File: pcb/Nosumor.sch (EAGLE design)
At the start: 111 parts, among them IC1 STM32F722RET, IC2 REG1117, IC3 TPS77018, J3 SJ-43515TS-SMT-EDGE, K1 CHERRY-MX, K2 CHERRY-MX, K3 KSC623J, K4 KSC623J, K5 KSC623J, Q1 CX2016DB, Q2 ABMM-6.000MHZ, Q3 FDY100PZ, Q4 FDY100PZ, Q5 FDY100PZ, Q6 FDY100PZ, U2 USB3370, U3 TLV320AIC3110

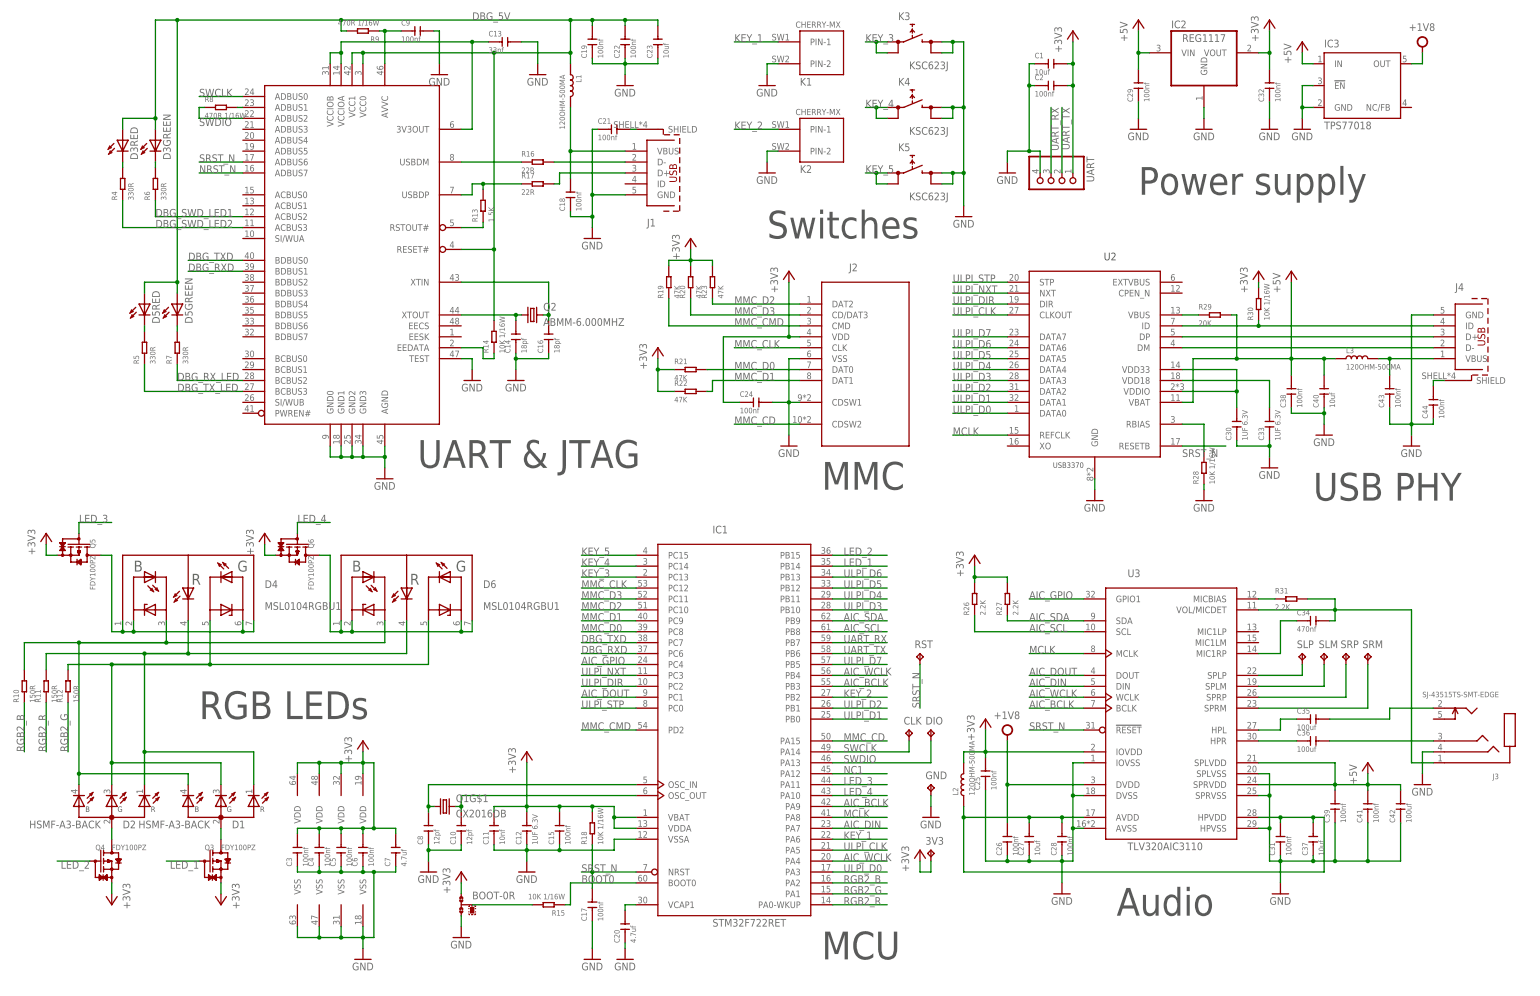
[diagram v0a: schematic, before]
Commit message: PCB: Connections done, update revision to 1.0
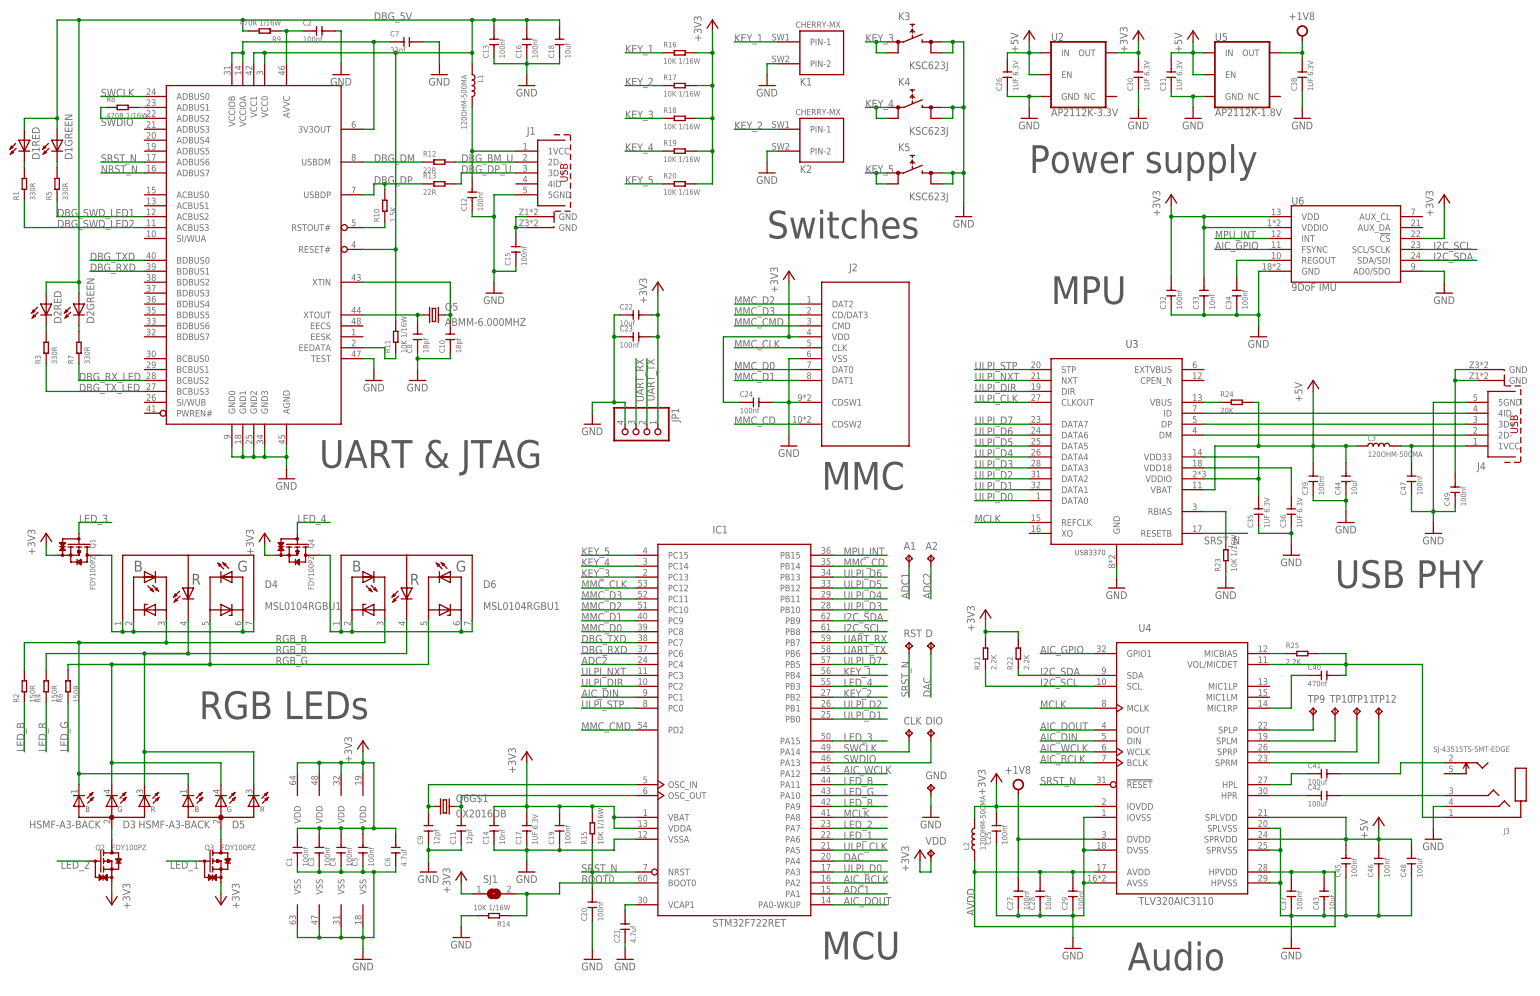
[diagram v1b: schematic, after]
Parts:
- removed BOOT: 0R-JUMPB, jump-0r-smd:0R-JUMPB
- removed IC2: REG1117, burr-brown:REG1117
- removed IC3: TPS77018, texas:TPS77018
- removed R26, R27, R31: 2.2K, Seeed-Resistor:SMD-RES-1K-5%-1/16W(0402)
- removed R28, R30: 10K 1/16W, Seeed-Resistor:SMD-RES-10K-1%-1/16W(0402)
- removed R29: 20K, Seeed-Resistor:SMD-RES-1K-5%-1/16W(0402)
- removed SLM, SLP, SRM, SRP: TPB1,27, testpad:TPB1,27
- removed UART: (no value), pinhead:PINHD-1X4
- added A1, A2, D, TP10, TP11, TP12, TP9: TPB1,27, testpad:TPB1,27
- added C45, C46, C47, C49: 100nf, Seeed-Capacitor:CERAMIC-100NF-25V-10%-X7R(0402)
- added C48: 100uf, Seeed-Capacitor:CERAMIC-100UF-6.3V-20%-X5R(1206)
- added JP1: (no value), pinhead:PINHD-1X4
- added R1, R3: 330R, Seeed-Resistor:SMD-RES-330R-1%-1/16W(0402)
- added R2: 150R, Seeed-Resistor:SMD-RES-330R-1%-1/16W(0402)
- added R24: 20K, Seeed-Resistor:SMD-RES-1K-5%-1/16W(0402)
- added R25: 2.2K, Seeed-Resistor:SMD-RES-1K-5%-1/16W(0402)
- added SJ1: (no value), jumper:SJ
- added U4: TLV320AIC3110, ti:TLV320AIC3110
- added U5: AP2112K-1.8V, SparkFun-IC-Power:V_REG_AP2112K-3.3V
- added U6: 9DoF IMU, SparkFun-Sensors:MPU-9250
- C1, C23, C27, C37: value 10uf -> 100nf; device Seeed-Capacitor:CERAMIC-10UF-10V-10%-X5R(0603) -> Seeed-Capacitor:CERAMIC-100NF-25V-10%-X7R(0402)
- C10, C8: value 12pf -> 18pf; device Seeed-Capacitor:CERAMIC-12PF-50V-5%-NPO(0402) -> Seeed-Capacitor:CERAMIC-18PF-50V-5%-NPO(0402)
- C11: value 10nf -> 12pf; device Seeed-Capacitor:CERAMIC-10NF-50V-10%-X7R(0402) -> Seeed-Capacitor:CERAMIC-12PF-50V-5%-NPO(0402)
- C12: value 1UF 6.3V -> 100nf; device Seeed-Capacitor:CERAMIC-1UF-6.3V-10%-X5R(0402) -> Seeed-Capacitor:CERAMIC-100NF-25V-10%-X7R(0402)
- C13: value 33nf -> 100nf; device Seeed-Capacitor:CERAMIC-22NF-50V-10%-X7R(0402) -> Seeed-Capacitor:CERAMIC-100NF-25V-10%-X7R(0402)
- C14: value 18pf -> 10nf; device Seeed-Capacitor:CERAMIC-18PF-50V-5%-NPO(0402) -> Seeed-Capacitor:CERAMIC-10NF-50V-10%-X7R(0402)
- C16: value 18pf -> 100nf; device Seeed-Capacitor:CERAMIC-18PF-50V-5%-NPO(0402) -> Seeed-Capacitor:CERAMIC-100NF-25V-10%-X7R(0402)
- C17, C26, C31, C38: value 100nf -> 1UF 6.3V; device Seeed-Capacitor:CERAMIC-100NF-25V-10%-X7R(0402) -> Seeed-Capacitor:CERAMIC-1UF-6.3V-10%-X5R(0402)
- C18, C22, C28, C43, C44: value 100nf -> 10uf; device Seeed-Capacitor:CERAMIC-100NF-25V-10%-X7R(0402) -> Seeed-Capacitor:CERAMIC-10UF-10V-10%-X5R(0603)
- C20: value 4.7uf -> 100nf; device Seeed-Capacitor:CERAMIC-4.7UF-10V-10%-X5R(0603) -> Seeed-Capacitor:CERAMIC-100NF-25V-10%-X7R(0402)
- C21, C6: value 100nf -> 4.7uf; device Seeed-Capacitor:CERAMIC-100NF-25V-10%-X7R(0402) -> Seeed-Capacitor:CERAMIC-4.7UF-10V-10%-X5R(0603)
- C33: value 1UF 6.3V -> 10nf; device Seeed-Capacitor:CERAMIC-1UF-6.3V-10%-X5R(0402) -> Seeed-Capacitor:CERAMIC-10NF-50V-10%-X7R(0402)
- C34: value 470nf -> 100nf; device Seeed-Capacitor:CERAMIC-47NF-25V-10%-X7R(0402) -> Seeed-Capacitor:CERAMIC-100NF-25V-10%-X7R(0402)
- C35, C36: value 100uf -> 1UF 6.3V; device Seeed-Capacitor:CERAMIC-100UF-6.3V-20%-X5R(1206) -> Seeed-Capacitor:CERAMIC-1UF-6.3V-10%-X5R(0402)
- C40: value 10uf -> 470nf; device Seeed-Capacitor:CERAMIC-10UF-10V-10%-X5R(0603) -> Seeed-Capacitor:CERAMIC-47NF-25V-10%-X7R(0402)
- C41: value 100nf -> 100uf; device Seeed-Capacitor:CERAMIC-100NF-25V-10%-X7R(0402) -> Seeed-Capacitor:CERAMIC-100UF-6.3V-20%-X5R(1206)
- C7: value 4.7uf -> 33nf; device Seeed-Capacitor:CERAMIC-4.7UF-10V-10%-X5R(0603) -> Seeed-Capacitor:CERAMIC-22NF-50V-10%-X7R(0402)
- C9: value 100nf -> 12pf; device Seeed-Capacitor:CERAMIC-100NF-25V-10%-X7R(0402) -> Seeed-Capacitor:CERAMIC-12PF-50V-5%-NPO(0402)
- D1, D2: value HSMF-A3-BACK -> APBD3224SURKCGKC-F01; device led:HSMF-A3-BACK -> led:APBD3224SURKCGKC-F01
- D3, D5: value APBD3224SURKCGKC-F01 -> HSMF-A3-BACK; device led:APBD3224SURKCGKC-F01 -> led:HSMF-A3-BACK
- J1, J4: device Wurth_Elektronik_Electromechanic_Input-Output_Connectors_rev17b:629105136821 -> Wurth_Elektronik_Electromechanic_Input-Output_Connectors_rev16b:629105150521
- Q1: value CX2016DB -> FDY100PZ; device crystal:CX2016DB -> transistor:FDY100PZ
- Q2: value ABMM-6.000MHZ -> FDY100PZ; device crystal:ABMM-6.000MHZ -> transistor:FDY100PZ
- Q5: value FDY100PZ -> ABMM-6.000MHZ; device transistor:FDY100PZ -> crystal:ABMM-6.000MHZ
- Q6: value FDY100PZ -> CX2016DB; device transistor:FDY100PZ -> crystal:CX2016DB
- R10: value 150R -> 1.5K; device Seeed-Resistor:SMD-RES-330R-1%-1/16W(0402) -> Seeed-Resistor:SMD-RES-1.5K-5%-1/16W(0402)
- R11: value 150R -> 10K 1/16W; device Seeed-Resistor:SMD-RES-330R-1%-1/16W(0402) -> Seeed-Resistor:SMD-RES-10K-1%-1/16W(0402)
- R12: value 150R -> 22R; device Seeed-Resistor:SMD-RES-330R-1%-1/16W(0402) -> Seeed-Resistor:SMD-RES-22R-1%-1/16W(0402)
- R13: value 1.5K -> 22R; device Seeed-Resistor:SMD-RES-1.5K-5%-1/16W(0402) -> Seeed-Resistor:SMD-RES-22R-1%-1/16W(0402)
- R16, R17: value 22R -> 10K 1/16W; device Seeed-Resistor:SMD-RES-22R-1%-1/16W(0402) -> Seeed-Resistor:SMD-RES-10K-1%-1/16W(0402)
- R19, R20, R23: value 47K -> 10K 1/16W; device Seeed-Resistor:SMD-RES-47K-5%-1/16W(0402) -> Seeed-Resistor:SMD-RES-10K-1%-1/16W(0402)
- R21, R22: value 47K -> 2.2K; device Seeed-Resistor:SMD-RES-47K-5%-1/16W(0402) -> Seeed-Resistor:SMD-RES-1K-5%-1/16W(0402)
- R4, R6: value 330R -> 150R
- U2: value USB3370 -> AP2112K-3.3V; device microchip:USB3370 -> SparkFun-IC-Power:V_REG_AP2112K-3.3V
- U3: value TLV320AIC3110 -> USB3370; device ti:TLV320AIC3110 -> microchip:USB3370
- renumbered 3V3 to VDD
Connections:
- removed net AIC_SCL: IC1G$1.PB8, R26.1, U3.SCL
- removed net AIC_SDA: IC1G$1.PB9, R27.1, U3.SDA
- removed net N$15: R16.1, U1.USBDM
- removed net N$16: J1.D+, R17.2
- removed net N$22: C21.2, J1.SHIELD
- removed net N$40: D1.KG, D2.KG, D4.KB, D6.KB, R12.2
- removed net N$41: D1.KR, D2.KR, D4.KR, D6.KR, R11.2
- removed net N$42: D1.KB, D2.KB, D4.KG, D6.KG, R10.2
- removed net N$51: C27.2, C28.2, C31.2, C37.2, L2.1, U3.AVDD, U3.HPVDD
- removed net N$8: J1.D-, R16.2
- removed net N$9: R13.2, R17.1, U1.USBDP
- removed net NC1: IC1G$1.PA12
- removed net RGB2_B: IC1G$1.PA2, R10.1
- removed net RGB2_G: IC1G$1.PA1, R12.1
- removed net RGB2_R: IC1G$1.PA0-WKUP, R11.1
- new net ADC1: A1.TP, IC1G$1.PA1
- new net ADC2: A2.TP, IC1G$1.PC4
- new net AVDD: C28.2, C29.2, C37.2, C43.2, L2.1, U4.AVDD, U4.HPVDD
- new net DAC: D.TP, IC1G$1.PA4
- new net DBG_BM_U: J1.2D-, R12.2
- new net DBG_DM: R12.1, U1.USBDM
- new net DBG_DP: R10.2, R13.1, U1.USBDP
- new net DBG_DP_U: J1.3D+, R13.2
- new net I2C_SCL: IC1G$1.PB8, R21.1, U4.SCL, U6.SCL/SCLK
- new net I2C_SDA: IC1G$1.PB9, R22.1, U4.SDA, U6.SDA/SDI
- new net LED_B: IC1G$1.PA11, R2.1
- new net LED_G: IC1G$1.PA10, R6.1
- new net LED_R: IC1G$1.PA9, R4.1
- new net MPU_INT: IC1G$1.PB15, U6.INT
- new net N$47: C34.2, U6.REGOUT
- new net RGB_B: D3.KB, D4.KG, D5.KB, D6.KG, R2.2
- new net RGB_G: D3.KG, D4.KB, D5.KG, D6.KB, R6.2
- new net RGB_R: D3.KR, D4.KR, D5.KR, D6.KR, R4.2
- net +1V8: now also C27.2, C38.2, U4.DVDD, U5.OUT; no longer C26.2, IC3.OUT, U3.DVDD
- net +3V3: now also C14.2, C17.2, C19.2, C22.2, C23.2, C30.2, C33.2, JP1.1, Q1.S, Q2.S, R15.2, R16.2, R17.2, R21.2, R22.2, SJ1.1, U2.OUT, U4.IOVDD, U6.!CS, U6.VDD, U6.VDDIO; no longer BOOT-0R.1, C11.2, C12.2, C15.2, C2.2, C7.2, IC2.VOUT, Q5.S, Q6.S, R21.1, R22.1, R23.2, R26.2, R27.2, R30.2, U3.IOVDD, UART.1
- net +5V: now also C26.2, C31.2, C44.2, C45.2, C46.2, C48.2, R24.2, U2.EN, U2.IN, U3.VBAT, U4.SPLVDD, U4.SPRVDD, U5.EN, U5.IN; no longer C29.2, C38.2, C40.2, C41.2, C42.2, IC2.VIN, IC3.IN, R29.2, U2.VBAT, U3.SPLVDD, U3.SPRVDD
- net AIC_BCLK: now also IC1G$1.PA2, U4.BCLK; no longer IC1G$1.PA9, IC1G$1.PB3, U3.BCLK
- net AIC_DIN: now also IC1G$1.PC1, U4.DIN; no longer IC1G$1.PA7, U3.DIN
- net AIC_DOUT: now also IC1G$1.PA0-WKUP, U4.DOUT; no longer IC1G$1.PC1, U3.DOUT
- net AIC_GPIO: now also U4.GPIO1, U6.FSYNC; no longer IC1G$1.PC4, U3.GPIO1
- net AIC_WCLK: now also IC1G$1.PA12, U4.WCLK; no longer IC1G$1.PA4, IC1G$1.PB4, U3.WCLK
- net BOOT0: now also R14.1, SJ1.2; no longer R15.1
- net DBG_5V: now also C13.2, C16.2, C18.2, D1GREEN.A, D1RED.A, D2GREEN.A, D2RED.A, R11.2; no longer C19.2, C22.2, C23.2, D3GREEN.A, D3RED.A, D5GREEN.A, D5RED.A, R14.2
- net DBG_SWD_LED1: now also R5.1; no longer R6.1
- net DBG_SWD_LED2: now also R1.1; no longer R4.1
- net DBG_TX_LED: now also R3.1; no longer R5.1
- net GND: now also C13.1, C2.2, C34.1, C35.1, C36.1, C45.1, C46.1, C47.1, C48.1, C49.1, C7.2, C9.1, J1.5GND, J4.5GND, JP1.4, R14.2, R23.1, U3.GND, U4.AVSS, U4.DVSS, U4.HPVSS, U4.IOVSS, U4.SPLVSS, U4.SPRVSS, U5.GND, U6.AD0/SDO, U6.GND; no longer BOOT-0R.3, C13.2, C2.1, C40.1, C41.1, C42.1, C7.1, C9.2, IC2.GND, IC3.!EN, IC3.GND, J1.GND, J4.GND, R28.1, U3.AVSS, U3.DVSS, U3.HPVSS, U3.IOVSS, U3.SPLVSS, U3.SPRVSS, UART.4
- net KEY_1: now also IC1G$1.PB4, R16.1; no longer IC1G$1.PA6
- net KEY_2: now also R17.1
- net KEY_3: now also R18.1
- net KEY_4: now also R19.1
- net KEY_5: now also R20.1
- net LED_1: now also IC1G$1.PA6; no longer IC1G$1.PB14
- net LED_2: now also IC1G$1.PA7, Q2.G; no longer IC1G$1.PB15, Q4.G
- net LED_3: now also IC1G$1.PA15, Q1.G; no longer IC1G$1.PA11, Q5.G
- net LED_4: now also IC1G$1.PB3, Q4.G; no longer IC1G$1.PA10, Q6.G
- net MCLK: now also U3.REFCLK, U4.MCLK; no longer U2.REFCLK, U3.MCLK
- net MMC_CD: now also IC1G$1.PB14; no longer IC1G$1.PA15
- net MMC_CMD: no longer R19.1
- net MMC_D0: no longer R21.2
- net MMC_D1: no longer R22.2
- net MMC_D2: no longer R23.1
- net MMC_D3: no longer R20.1
- net N$1: now also C41.2; no longer C35.2
- net N$10: now also C7.1; no longer C13.1
- net N$11: now also C2.1; no longer C9.1
- net N$12: now also D1GREEN.C, R5.2; no longer D3GREEN.C, R6.2
- net N$13: now also C12.2, J1.1VCC; no longer C18.2, J1.VBUS
- net N$14: now also R10.1; no longer R13.1
- net N$17: now also R11.1; no longer R14.1
- net N$18: now also C8.2, Q5.1; no longer C14.2, Q2.1
- net N$19: now also C10.2, Q5.2; no longer C16.2, Q2.2
- net N$2: now also C42.2; no longer C36.2
- net N$20: now also D2GREEN.C; no longer D5GREEN.C
- net N$21: now also D2RED.C, R3.2; no longer D5RED.C, R5.2
- net N$23: now also D1RED.C, R1.2; no longer D3RED.C, R4.2
- net N$24: now also C9.2, Q6G$1.1; no longer C8.2, Q1G$1.1
- net N$26: now also C11.2, Q6G$1.2; no longer C10.2, Q1G$1.2
- net N$27: now also C15.2, J1.GND@1, J1.GND@2; no longer BOOT-0R.2, R15.2
- net N$28: now also Q4.D; no longer Q6.D
- net N$29: now also C21.2; no longer C20.2
- net N$3: now also C40.2, R25.2, U4.VOL/MICDET; no longer C34.2, R31.2, U3.VOL/MICDET
- net N$30: now also TP10.TP, U4.SPLM; no longer SLM.TP, U3.SPLM
- net N$31: now also C47.2, J4.1VCC; no longer C43.2, J4.VBUS
- net N$32: now also R24.1, U3.VBUS; no longer R29.1, U2.VBUS
- net N$33: now also C35.2, U3.VDD33, U3.VDDIO; no longer C30.2, U2.VDD33, U2.VDDIO
- net N$34: now also D5.A; no longer D1.A
- net N$35: now also C49.2, J4.GND@1, J4.GND@2; no longer C44.2, J4.SHIELD
- net N$36: now also C36.2, U3.VDD18; no longer C33.2, U2.VDD18
- net N$37: now also R23.2, U3.RBIAS; no longer R28.2, U2.RBIAS
- net N$38: now also Q1.D; no longer Q5.D
- net N$39: now also D3.A, Q2.D; no longer D2.A, Q4.D
- net N$4: now also J4.2D-, U3.DM; no longer J4.D+, U2.DP
- net N$44: now also TP11.TP, U4.SPRP; no longer SRP.TP, U3.SPRP
- net N$45: now also TP12.TP, U4.SPRM; no longer SRM.TP, U3.SPRM
- net N$46: now also C40.1, U4.MIC1RP; no longer C34.1, U3.MIC1RP
- net N$48: now also C42.1, U4.HPR; no longer C36.1, U3.HPR
- net N$49: now also R25.1, U4.MICBIAS; no longer R31.1, U3.MICBIAS
- net N$5: now also J4.3D+, U3.DP; no longer J4.D-, U2.DM
- net N$50: now also C41.1, U4.HPL; no longer C35.1, U3.HPL
- net N$6: now also J4.4ID, U3.ID; no longer J4.ID, R30.1, U2.ID
- net N$7: now also TP9.TP, U4.SPLP; no longer SLP.TP, U3.SPLP
- net SRST_N: now also C20.2, R15.1, U3.RESETB, U4.!RESET; no longer C17.2, R18.1, U2.RESETB, U3.!RESET
- net UART_RX: now also JP1.3; no longer UART.3
- net UART_TX: now also JP1.2; no longer UART.2
- net ULPI_CLK: now also U3.CLKOUT; no longer U2.CLKOUT
- net ULPI_D0: now also U3.DATA0; no longer U2.DATA0
- net ULPI_D1: now also U3.DATA1; no longer U2.DATA1
- net ULPI_D2: now also U3.DATA2; no longer U2.DATA2
- net ULPI_D3: now also U3.DATA3; no longer U2.DATA3
- net ULPI_D4: now also U3.DATA4; no longer U2.DATA4
- net ULPI_D5: now also U3.DATA5; no longer U2.DATA5
- net ULPI_D6: now also U3.DATA6; no longer U2.DATA6
- net ULPI_D7: now also U3.DATA7; no longer U2.DATA7
- net ULPI_DIR: now also U3.DIR; no longer U2.DIR
- net ULPI_NXT: now also U3.NXT; no longer U2.NXT
- net ULPI_STP: now also U3.STP; no longer U2.STP
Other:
- note added: "MPU"
- moved on the sheet: C1, C10, C11, C12, C13, C14, C15, C16, C17, C18, C19, C2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

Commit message: PCB: Revision 1.0, silkscreen checked
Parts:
- added GND$2, SCL, SDA: TPB1,27, testpad:TPB1,27
- renumbered SJ1 to BOOT, TP10 to SLM, TP11 to SRP, TP12 to SRM, TP9 to SLP
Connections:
- net GND: now also GND$2.TP
- net I2C_SCL: now also SCL.TP
- net I2C_SDA: now also SDA.TP
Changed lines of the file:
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@@
 <part name="P+2" library="supply1" library_urn="urn:adsk.eagle:library:371" deviceset="+5V" device=""/>
 <part name="V2" library="supply" deviceset="+1V8" device=""/>
-<part name="TP9" library="testpad" library_urn="urn:adsk.eagle:library:385" deviceset="TP" device="B1,27" package3d_urn="urn:adsk.eagle:package:27944/1"/>
-<part name="TP10" library="testpad" library_urn="urn:adsk.eagle:library:385" deviceset="TP" device="B1,27" package3d_urn="urn:adsk.eagle:package:27944/1"/>
-<part name="TP11" library="testpad" library_urn="urn:adsk.eagle:library:385" deviceset="TP" device="B1,27" package3d_urn="urn:adsk.eagle:package:27944/1"/>
-<part name="TP12" library="testpad" library_urn="urn:adsk.eagle:library:385" deviceset="TP" device="B1,27" package3d_urn="urn:adsk.eagle:package:27944/1"/>
+<part name="SLP" library="testpad" library_urn="urn:adsk.eagle:library:385" deviceset="TP" device="B1,27" package3d_urn="urn:adsk.eagle:package:27944/1"/>
+<part name="SLM" library="testpad" library_urn="urn:adsk.eagle:library:385" deviceset="TP" device="B1,27" package3d_urn="urn:adsk.eagle:package:27944/1"/>
+<part name="SRP" library="testpad" library_urn="urn:adsk.eagle:library:385" deviceset="TP" device="B1,27" package3d_urn="urn:adsk.eagle:package:27944/1"/>
+<part name="SRM" library="testpad" library_urn="urn:adsk.eagle:library:385" deviceset="TP" device="B1,27" package3d_urn="urn:adsk.eagle:package:27944/1"/>
 <part name="C40" library="Seeed-Capacitor" library_urn="urn:adsk.eagle:library:464" deviceset="CERAMIC-47NF-25V-10%-X7R(0402)" device="" value="470nf"/>
 <part name="R25" library="Seeed-Resistor" library_urn="urn:adsk.eagle:library:474" deviceset="SMD-RES-1K-5%-1/16W(0402)" device="" value="2.2K"/>
@@
 <part name="R16" library="Seeed-Resistor" library_urn="urn:adsk.eagle:library:474" deviceset="SMD-RES-10K-1%-1/16W(0402)" device="" value="10K 1/16W"/>
 <part name="+3V39" library="supply1" library_urn="urn:adsk.eagle:library:371" deviceset="+3V3" device=""/>
-<part name="SJ1" library="jumper" library_urn="urn:adsk.eagle:library:252" deviceset="SJ" device="" package3d_urn="urn:adsk.eagle:package:15471/1"/>
+<part name="BOOT" library="jumper" library_urn="urn:adsk.eagle:library:252" deviceset="SJ" device="" package3d_urn="urn:adsk.eagle:package:15471/1"/>
 <part name="J4" library="Wurth_Elektronik_Electromechanic_Input-Output_Connectors_rev16b" deviceset="629105150521" device=""/>
 <part name="J1" library="Wurth_Elektronik_Electromechanic_Input-Output_Connectors_rev16b" deviceset="629105150521" device=""/>
@@
 <part name="GND29" library="supply1" library_urn="urn:adsk.eagle:library:371" deviceset="GND" device=""/>
 <part name="C31" library="Seeed-Capacitor" library_urn="urn:adsk.eagle:library:464" deviceset="CERAMIC-1UF-6.3V-10%-X5R(0402)" device="" value="1UF 6.3V"/>
+<part name="SDA" library="testpad" library_urn="urn:adsk.eagle:library:385" deviceset="TP" device="B1,27" package3d_urn="urn:adsk.eagle:package:27944/1"/>
+<part name="SCL" library="testpad" library_urn="urn:adsk.eagle:library:385" deviceset="TP" device="B1,27" package3d_urn="urn:adsk.eagle:package:27944/1"/>
+<part name="GND$2" library="testpad" library_urn="urn:adsk.eagle:library:385" deviceset="TP" device="B1,27" package3d_urn="urn:adsk.eagle:package:27944/1"/>
 </parts>
 <sheets>
@@
 <instance part="P+2" gate="1" x="86.36" y="111.76"/>
 <instance part="V2" gate="G$1" x="111.76" y="111.76"/>
-<instance part="TP9" gate="G$1" x="114.3" y="-45.72"/>
-<instance part="TP10" gate="G$1" x="119.38" y="-45.72"/>
-<instance part="TP11" gate="G$1" x="124.46" y="-45.72"/>
-<instance part="TP12" gate="G$1" x="129.54" y="-45.72"/>
+<instance part="SLP" gate="G$1" x="114.3" y="-45.72"/>
+<instance part="SLM" gate="G$1" x="119.38" y="-45.72"/>
+<instance part="SRP" gate="G$1" x="124.46" y="-45.72"/>
+<instance part="SRM" gate="G$1" x="129.54" y="-45.72"/>
 <instance part="C40" gate="G$1" x="116.84" y="-38.1"/>
 <instance part="R25" gate="G$1" x="111.76" y="-33.02"/>
@@
 <instance part="R16" gate="G$1" x="-33.02" y="106.68"/>
 <instance part="+3V39" gate="G$1" x="-25.4" y="114.3"/>
-<instance part="SJ1" gate="1" x="-76.2" y="-88.9"/>
+<instance part="BOOT" gate="1" x="-76.2" y="-88.9"/>
 <instance part="J4" gate="G$1" x="157.48" y="20.32" rot="MR180"/>
 <instance part="J1" gate="G$1" x="-63.5" y="78.74"/>
@@
 <instance part="GND29" gate="1" x="111.76" y="91.44"/>
 <instance part="C31" gate="G$1" x="81.28" y="101.6" rot="R90"/>
+<instance part="SDA" gate="G$1" x="-50.8" y="10.16"/>
+<instance part="SCL" gate="G$1" x="-43.18" y="10.16"/>
+<instance part="GND$2" gate="G$1" x="-35.56" y="10.16"/>
 </instances>
 <busses>
@@
 <pinref part="C38" gate="G$1" pin="1"/>
 </segment>
+<segment>
+<pinref part="GND$2" gate="G$1" pin="TP"/>
+<wire x1="-35.56" y1="7.62" x2="-35.56" y2="-2.54" width="0.1524" layer="91"/>
+<label x="-35.56" y="-2.54" size="1.778" layer="95" rot="R90"/>
+</segment>
 </net>
 <net name="+3V3" class="0">
@@
 <pinref part="+3V36" gate="G$1" pin="+3V3"/>
 <wire x1="-83.82" y1="-88.9" x2="-83.82" y2="-86.36" width="0.1524" layer="91"/>
-<pinref part="SJ1" gate="1" pin="1"/>
+<pinref part="BOOT" gate="1" pin="1"/>
 <wire x1="-81.28" y1="-88.9" x2="-83.82" y2="-88.9" width="0.1524" layer="91"/>
 </segment>
@@
 <label x="-55.88" y="-86.36" size="1.778" layer="95"/>
 <wire x1="-60.96" y1="-86.36" x2="-60.96" y2="-88.9" width="0.1524" layer="91"/>
-<pinref part="SJ1" gate="1" pin="2"/>
+<pinref part="BOOT" gate="1" pin="2"/>
 <wire x1="-71.12" y1="-88.9" x2="-68.58" y2="-88.9" width="0.1524" layer="91"/>
 <wire x1="-68.58" y1="-88.9" x2="-68.58" y2="-93.98" width="0.1524" layer="91"/>
@@
 <net name="N$7" class="0">
 <segment>
-<pinref part="TP9" gate="G$1" pin="TP"/>
+<pinref part="SLP" gate="G$1" pin="TP"/>
 <wire x1="114.3" y1="-48.26" x2="114.3" y2="-50.8" width="0.1524" layer="91"/>
 <pinref part="U4" gate="G$1" pin="SPLP"/>
@@
 <segment>
 <pinref part="U4" gate="G$1" pin="SPLM"/>
-<pinref part="TP10" gate="G$1" pin="TP"/>
+<pinref part="SLM" gate="G$1" pin="TP"/>
 <wire x1="104.14" y1="-53.34" x2="119.38" y2="-53.34" width="0.1524" layer="91"/>
 <wire x1="119.38" y1="-53.34" x2="119.38" y2="-48.26" width="0.1524" layer="91"/>
@@
 <segment>
 <pinref part="U4" gate="G$1" pin="SPRP"/>
-<pinref part="TP11" gate="G$1" pin="TP"/>
+<pinref part="SRP" gate="G$1" pin="TP"/>
 <wire x1="104.14" y1="-55.88" x2="124.46" y2="-55.88" width="0.1524" layer="91"/>
 <wire x1="124.46" y1="-55.88" x2="124.46" y2="-48.26" width="0.1524" layer="91"/>
@@
 <segment>
 <pinref part="U4" gate="G$1" pin="SPRM"/>
-<pinref part="TP12" gate="G$1" pin="TP"/>
+<pinref part="SRM" gate="G$1" pin="TP"/>
 <wire x1="104.14" y1="-58.42" x2="129.54" y2="-58.42" width="0.1524" layer="91"/>
 <wire x1="129.54" y1="-58.42" x2="129.54" y2="-48.26" width="0.1524" layer="91"/>
@@
 <label x="142.24" y="58.42" size="1.778" layer="95"/>
 </segment>
+<segment>
+<pinref part="SDA" gate="G$1" pin="TP"/>
+<wire x1="-50.8" y1="7.62" x2="-50.8" y2="-2.54" width="0.1524" layer="91"/>
+<label x="-50.8" y="-2.54" size="1.778" layer="95" rot="R90"/>
+</segment>
 </net>
 <net name="I2C_SCL" class="0">
@@
 <label x="142.24" y="60.96" size="1.778" layer="95"/>
 </segment>
+<segment>
+<pinref part="SCL" gate="G$1" pin="TP"/>
+<wire x1="-43.18" y1="7.62" x2="-43.18" y2="-2.54" width="0.1524" layer="91"/>
+<label x="-43.18" y="-2.54" size="1.778" layer="95" rot="R90"/>
+</segment>
 </net>
 <net name="AIC_DOUT" class="0">
@@
 <wire x1="104.14" y1="60.96" x2="91.44" y2="60.96" width="0.1524" layer="91"/>
 <label x="91.44" y="60.96" size="1.778" layer="95"/>
+<wire x1="104.14" y1="60.96" x2="91.44" y2="60.96" width="0.1524" layer="91"/>
 </segment>
 </net>
@@
 <wire x1="104.14" y1="63.5" x2="91.44" y2="63.5" width="0.1524" layer="91"/>
 <label x="91.44" y="63.5" size="1.778" layer="95"/>
-</segment>
-<segment>
+<wire x1="104.14" y1="63.5" x2="91.44" y2="63.5" width="0.1524" layer="91"/>
+</segment>
+<segment>
